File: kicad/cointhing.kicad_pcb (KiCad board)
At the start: 4 copper layers, 30 x 30 mm, 24 parts, among them J1 USB_B_Micro, Q1 PUMX1, Q2 S8050_J3Y, U1 ESP-12E, U2 CP2102-GMR_NRND, U3 BL8565, U4 74AHC1G08

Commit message: second pcb
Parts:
- removed LED1: WS2812B, LED_SMD:LED_WS2812B_PLCC4_5.0x5.0mm_P3.2mm
- added D1: WS2812B-2020, barn53-kicad:WS2812B-2020, B.Cu at (162.5, 71.0)
- added REF**: hole, hole, F.Cu at (154.5, 63.0)
- C4, C6, C7, C8, C9, R1, R3: moved to F.Cu
- moved R7 60.3 mm to (148.5, 78.0)
- moved U4 60.3 mm to (148.5, 81.0)
- moved J1 52.5 mm to (162.5, 60.1)
- moved C5 51.4 mm to (166.0, 73.5), turned to 90 degrees
- moved C2 50.9 mm to (175.0, 61.0)
- moved C3 50.9 mm to (175.0, 59.0)
- moved U1 48.3 mm to (165.5, 77.0), turned to 270 degrees
- moved C1 47.5 mm to (171.5, 59.0), turned to 0 degrees
- moved U2 44.6 mm to (174.5, 60.5), turned to 180 degrees
- moved Q1 43.8 mm to (167.0, 65.5)
- moved D2 42.6 mm to (162.5, 78.0)
- moved C6 41.1 mm to (148.5, 69.5), turned to 180 degrees
- moved C7 41.1 mm to (148.5, 67.5), turned to 180 degrees
- moved Q2 40.2 mm to (171.5, 69.0), turned to 90 degrees
- moved R6 40.1 mm to (172.5, 73.5), turned to 270 degrees
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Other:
- board size 30 x 30 mm -> 35 x 32 mm

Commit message: Wired PCB rev.B
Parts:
- added QR*****: https://barn53.github.io/CoinThing/, https://barn53.github.io/CoinThing/, B.Cu at (152.5, 76.9)
- moved C3 10.9 mm to (168.7, 67.9)
- moved R6 9.63 mm to (165.4, 80.0)
- moved C2 7.98 mm to (168.7, 65.9)
- moved D2 7.50 mm to (162.5, 85.5)
- moved C5 7.20 mm to (162.9, 80.0)
- moved Q2 7.20 mm to (168.4, 75.5)
- moved R5 7.20 mm to (167.4, 80.0)
- moved R4 6.56 mm to (169.4, 80.0)
- moved C1 5.64 mm to (168.7, 63.9), turned to 180 degrees
- moved U1 1.70 mm to (165.5, 78.7)
- moved C4 1.00 mm to (148.5, 72.5)
- moved C6 1.00 mm to (148.5, 70.5)
- moved C7 1.00 mm to (148.5, 68.5)
- moved C8 1.00 mm to (148.5, 66.5)
- moved C9 1.00 mm to (148.5, 64.5)
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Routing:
- net +3V3: track 0.00 -> 74.9 mm, vias 0 -> 6
- net VBUS: track 0.00 -> 58.8 mm, vias 0 -> 7
- net /TxD: track 0.00 -> 51.0 mm, vias 0 -> 4
- net /VDD: track 0.00 -> 32.7 mm, vias 0 -> 5
- net /~Reset: track 0.00 -> 30.9 mm, vias 0 -> 3
- net Net-(R1-Pad8): track 0.00 -> 30.6 mm, vias 0 -> 2
- net /GPIO0: track 0.00 -> 30.2 mm, vias 0 -> 2
- net /GPIO5: track 0.00 -> 28.9 mm, vias 0 -> 2
- net /RxD: track 0.00 -> 26.7 mm
- net Net-(R1-Pad5): track 0.00 -> 25.1 mm, vias 0 -> 2
- net /~TFT_RES: track 0.00 -> 25.0 mm, vias 0 -> 1
- net Net-(D1-Pad3): track 0.00 -> 22.1 mm, vias 0 -> 1
- net /DTR: track 0.00 -> 20.6 mm, vias 0 -> 4
- net /D-: track 0.00 -> 19.9 mm, vias 0 -> 2
- net /TFT_SDA: track 0.00 -> 19.6 mm, vias 0 -> 1
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- added copper zone on B.Cu, net GND
- added copper zone on F.Cu, net GND
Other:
- board size 35 x 32 mm -> 35 x 34 mm
- copper layers 4 -> 2
- net class Default: via_dia 0.6 -> 0.45; via_drill 0.3 -> 0.2
- net class Power: clearance 0.254 -> 0.1524
- board text added: "CoinThing a coin ticker display"
- board text added: "CoinThing barn53 rev.B 02/21"
- board text added: "To the Moon!"

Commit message: Rev.B PCB
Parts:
- QR*****: footprint https://barn53.github.io/CoinThing/ -> https:__barn53.github.io_CoinThing_
- moved U3 2.10 mm to (149.0, 61.6)
- moved C4 1.80 mm to (148.5, 74.3)
- moved C6 1.80 mm to (148.5, 72.3)
- moved C7 1.80 mm to (148.5, 70.3)
- moved C8 1.80 mm to (148.5, 68.3)
- moved C9 1.80 mm to (148.5, 66.3)
- moved J1 0.18 mm to (162.5, 59.9)
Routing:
- net VBUS: track 58.8 -> 61.8 mm
- net Net-(R1-Pad6): track 17.1 -> 18.4 mm
- net Net-(D1-Pad3): track 22.1 -> 20.9 mm
- net Net-(R1-Pad5): track 25.1 -> 26.1 mm
- net /~Reset: track 30.9 -> 31.9 mm
- net +3V3: track 74.9 -> 75.7 mm
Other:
- outline, holes or cut-outs redrawn
- board text added: "CoinThing"

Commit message: Added second mounting hole to PCB, rearranged parts a bit
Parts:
- added REF**: hole, hole, F.Cu at (175.0, 59.9)
- moved U3 5.70 mm to (154.5, 63.1)
- moved REF** 5.46 mm to (150.0, 59.9)
- moved U2 4.55 mm to (175.2, 65.9)
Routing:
- net Net-(R1-Pad8): track 31.0 -> 25.4 mm
- net /RTS: track 16.1 -> 21.4 mm, vias 2 -> 5
- net VBUS: track 61.8 -> 56.9 mm, vias 7 -> 8
- net /D+: track 18.5 -> 23.2 mm, vias 2 -> 4
- net /RxD: track 26.7 -> 23.0 mm
- net /TxD: track 51.0 -> 47.3 mm
- net +3V3: track 75.7 -> 78.8 mm, vias 6 -> 7
- net /D-: track 20.0 -> 21.9 mm, vias 2 -> 4
- net Net-(R1-Pad5): track 26.1 -> 25.5 mm
- net /VDD: track 32.7 -> 33.3 mm
- net /GPIO0: track 30.2 -> 30.7 mm
- net GND: vias 6 -> 13
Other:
- board text added: "CoinThing barn53 rev.C 02/21"
- board text removed: "CoinThing barn53 rev.B 02/21"

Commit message: modified PCB wiring
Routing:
- net /VDD: track 33.3 -> 29.4 mm, vias 5 -> 4
- net Net-(R1-Pad6): track 18.3 -> 14.7 mm, vias 4 -> 2
- net +3V3: track 78.8 -> 77.3 mm, vias 7 -> 8

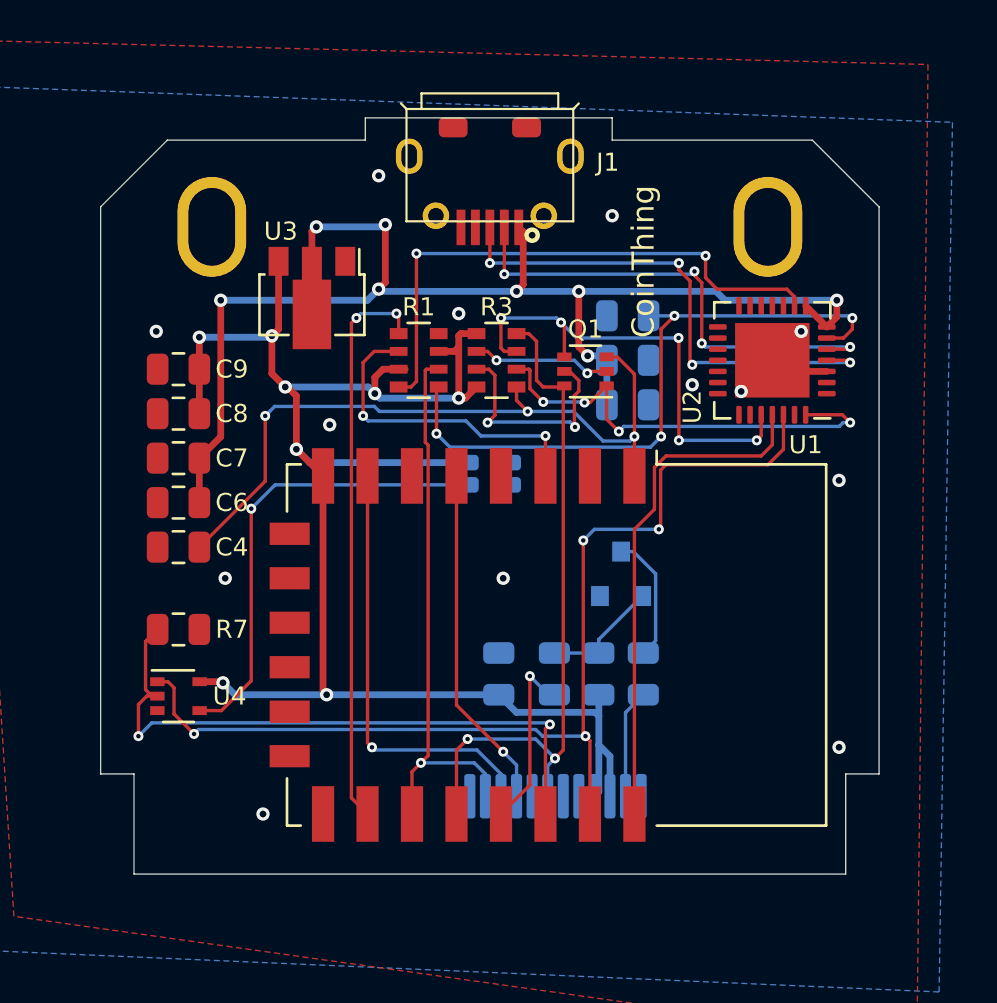
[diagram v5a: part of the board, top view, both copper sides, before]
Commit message: PCB completely new part arrangement
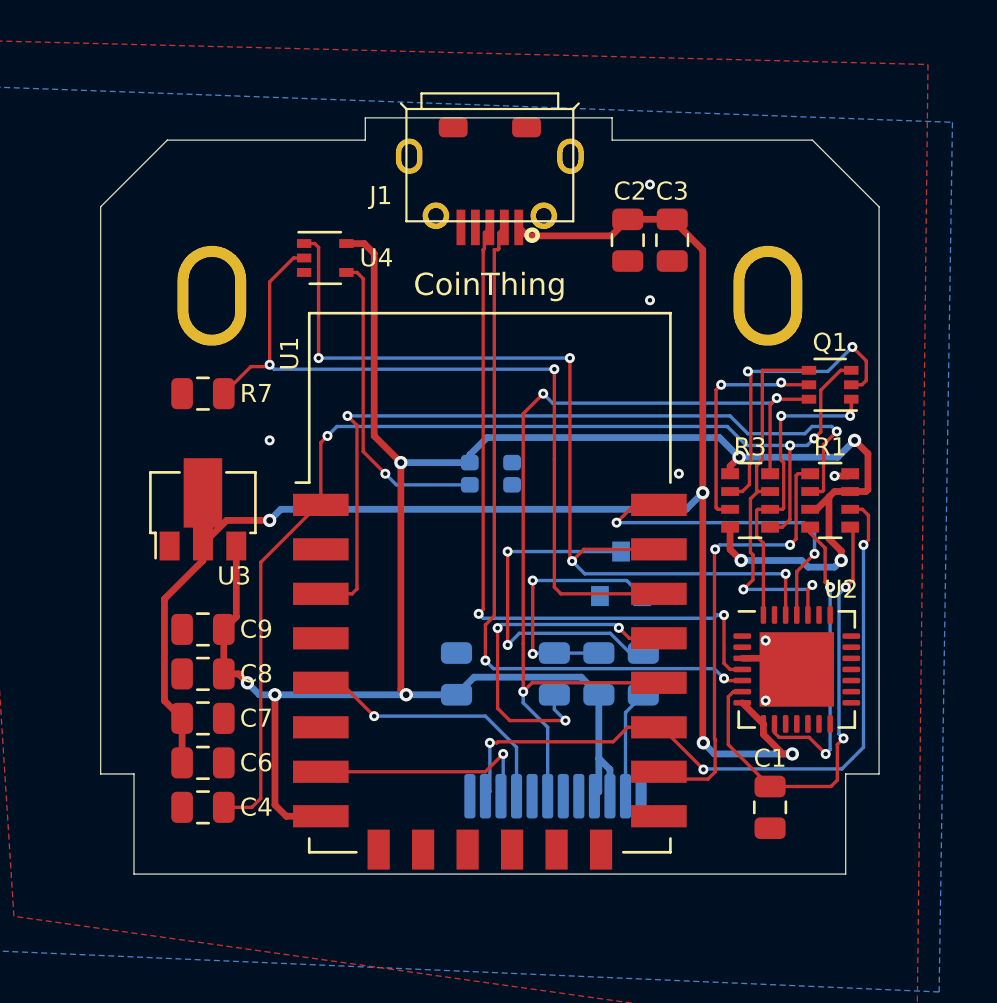
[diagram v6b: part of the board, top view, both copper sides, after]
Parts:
- C1, C2, C3: moved to F.Cu
- moved C1 23.0 mm to (175.1, 86.0), turned to 270 degrees
- moved U4 20.8 mm to (155.1, 61.3)
- moved R1 19.5 mm to (177.8, 72.2)
- moved U2 13.9 mm to (176.3, 79.8), turned to 0 degrees
- moved R3 13.0 mm to (174.2, 72.2)
- moved C4 11.8 mm to (149.6, 86.0)
- moved C6 11.8 mm to (149.6, 84.0), turned to 0 degrees
- moved C7 11.8 mm to (149.6, 82.0), turned to 0 degrees
- moved C8 11.8 mm to (149.6, 80.0)
- moved C9 11.8 mm to (149.6, 78.0)
- moved Q1 11.0 mm to (177.8, 67.0)
- moved U3 10.7 mm to (149.6, 72.6), turned to 90 degrees
- moved R7 10.7 mm to (149.6, 67.4), turned to 180 degrees
- moved C3 7.67 mm to (170.7, 60.5), turned to 270 degrees
- moved C2 5.40 mm to (168.7, 60.5), turned to 270 degrees
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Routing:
- net Net-(R1-Pad6): track 14.7 -> 35.8 mm
- net +3V3: track 77.3 -> 97.2 mm
- net /~Reset: track 32.1 -> 50.4 mm
- net VBUS: track 57.3 -> 73.5 mm, vias 8 -> 4
- net Net-(R1-Pad8): track 25.4 -> 13.7 mm
- net Net-(Q2-Pad3): track 5.76 -> 16.0 mm, vias 0 -> 2
- net /GPIO0: track 30.7 -> 41.0 mm, vias 2 -> 3
- net /D-: track 21.9 -> 31.8 mm, vias 4 -> 2
- net /TFT_SDA: track 19.6 -> 10.5 mm
- net /VDD: track 29.4 -> 20.6 mm, vias 4 -> 2
- net /D+: track 23.2 -> 31.9 mm, vias 4 -> 2
- net /RxD: track 23.0 -> 15.3 mm, vias 0 -> 2
- net /TFT_BL: track 8.19 -> 15.8 mm, vias 1 -> 3
- net Net-(Q1-Pad2): track 6.29 -> 13.8 mm
- net /~TFT_RES: track 25.0 -> 32.2 mm, vias 1 -> 3
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
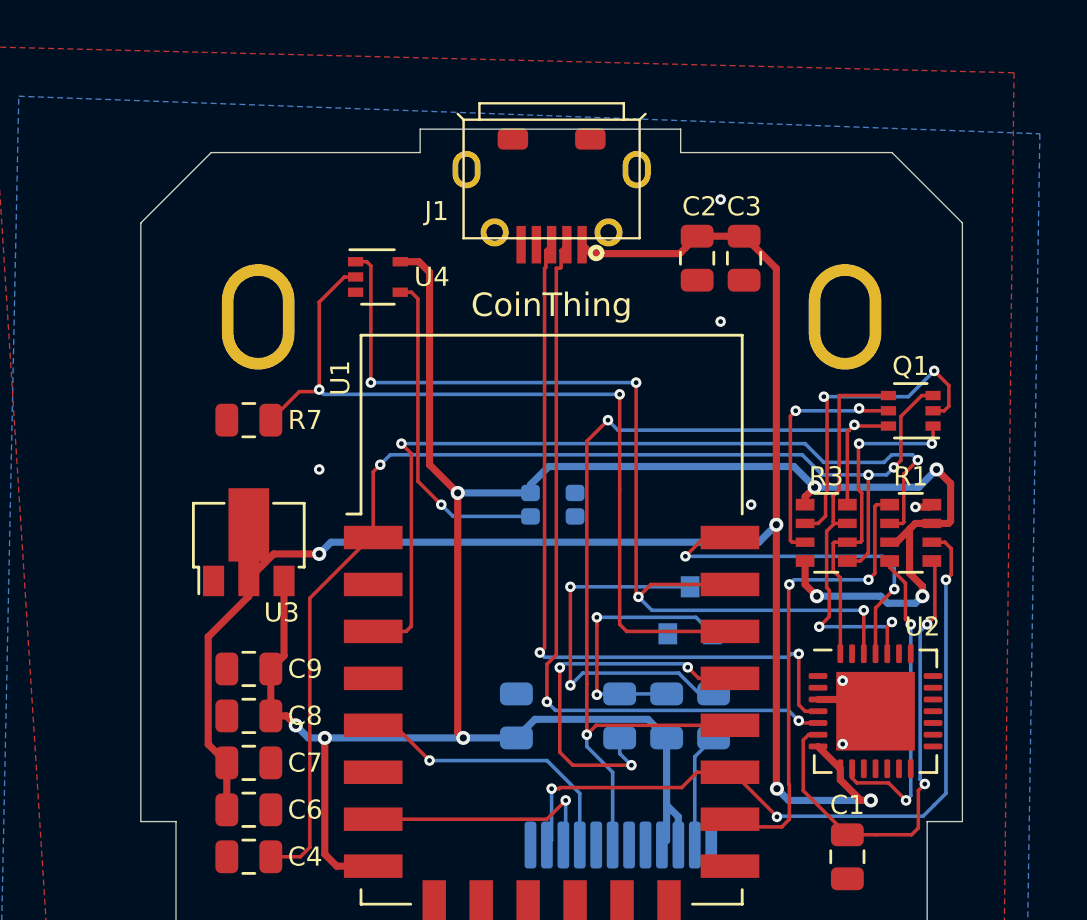
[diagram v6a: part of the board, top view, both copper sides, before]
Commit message: Moved USB to the side
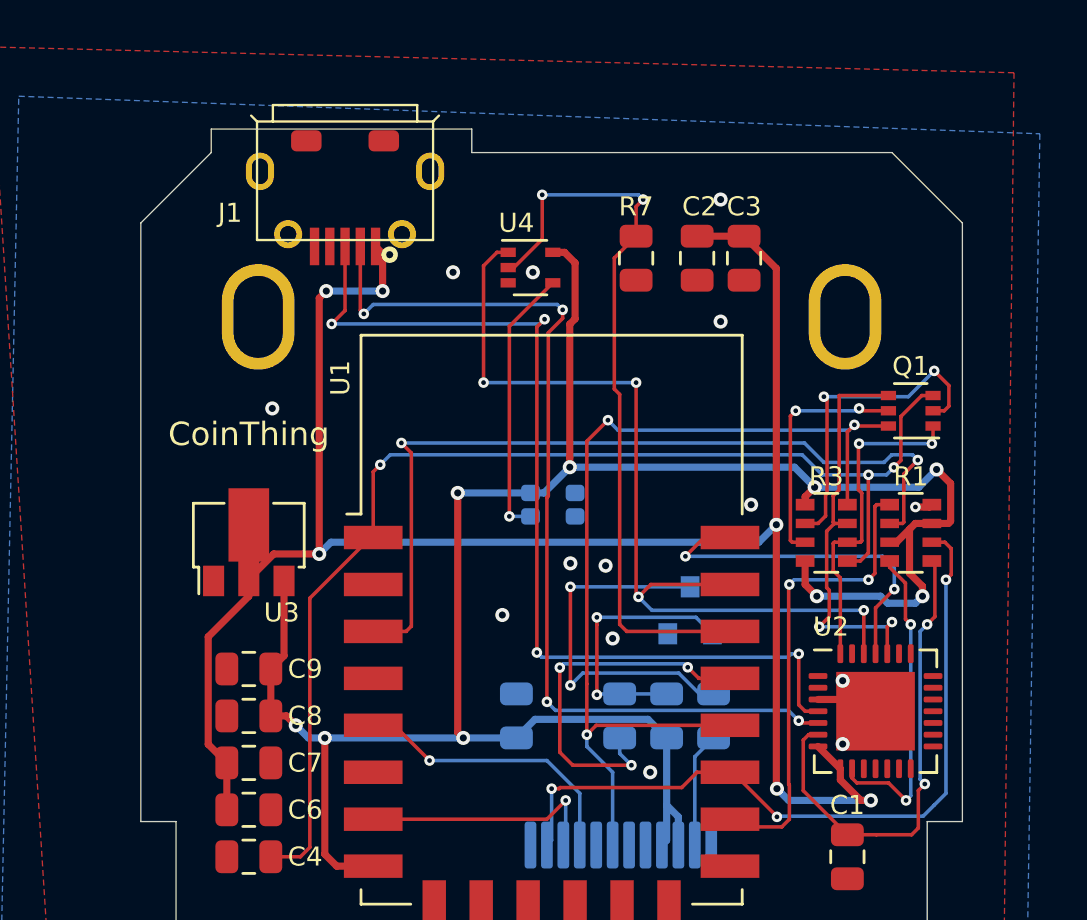
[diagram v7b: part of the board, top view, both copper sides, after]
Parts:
- moved R7 17.9 mm to (166.1, 60.5), turned to 270 degrees
- moved J1 8.80 mm to (153.7, 60.0)
- moved U4 6.51 mm to (161.6, 60.9)
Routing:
- net VBUS: track 73.5 -> 83.9 mm, vias 4 -> 6
- net /D+: track 31.9 -> 41.5 mm, vias 2 -> 4
- net /D-: track 31.8 -> 40.6 mm, vias 2 -> 4
- net /TxD: track 42.0 -> 37.7 mm
- net /GPIO5: track 35.8 -> 31.8 mm
- net Net-(D1-Pad3): track 14.1 -> 11.6 mm
- net +3V3: track 97.2 -> 95.5 mm, vias 8 -> 9
- net GND: vias 7 -> 14
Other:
- outline, holes or cut-outs redrawn

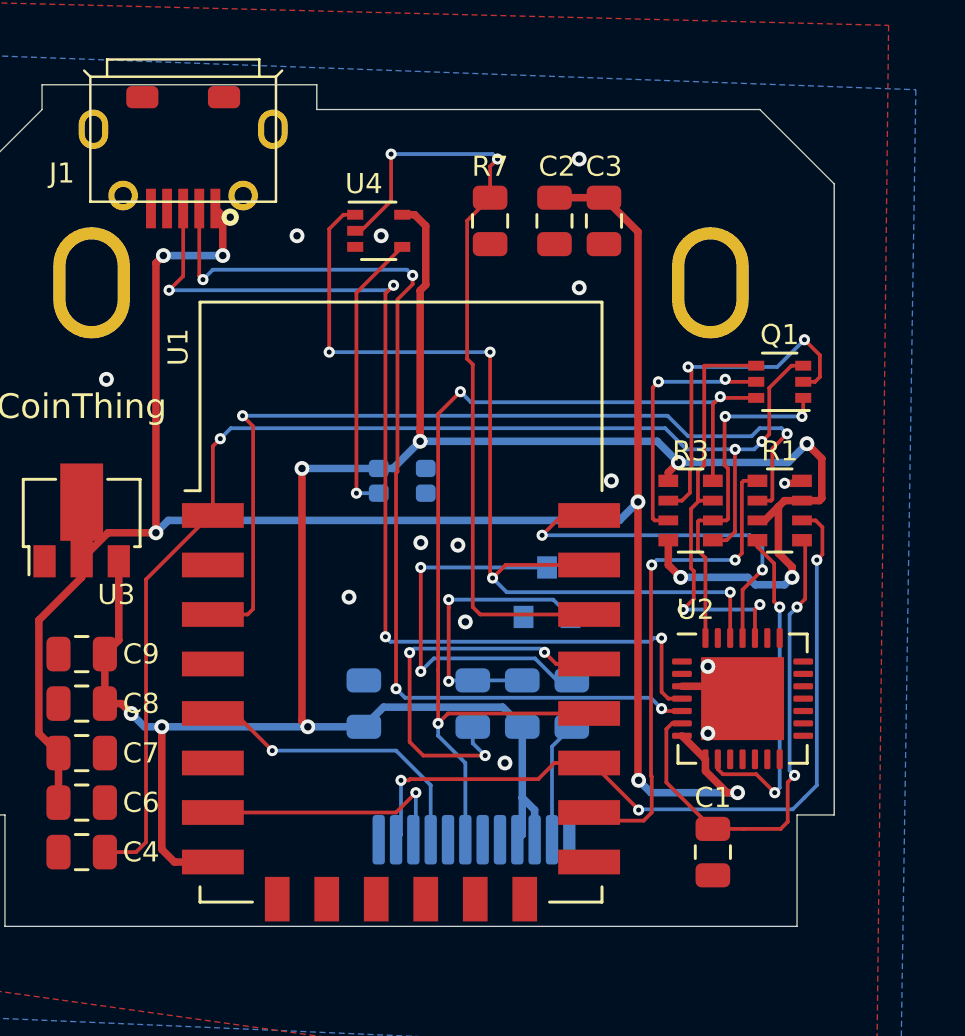
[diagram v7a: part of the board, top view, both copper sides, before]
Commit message: moved led to the center of the bottom plane
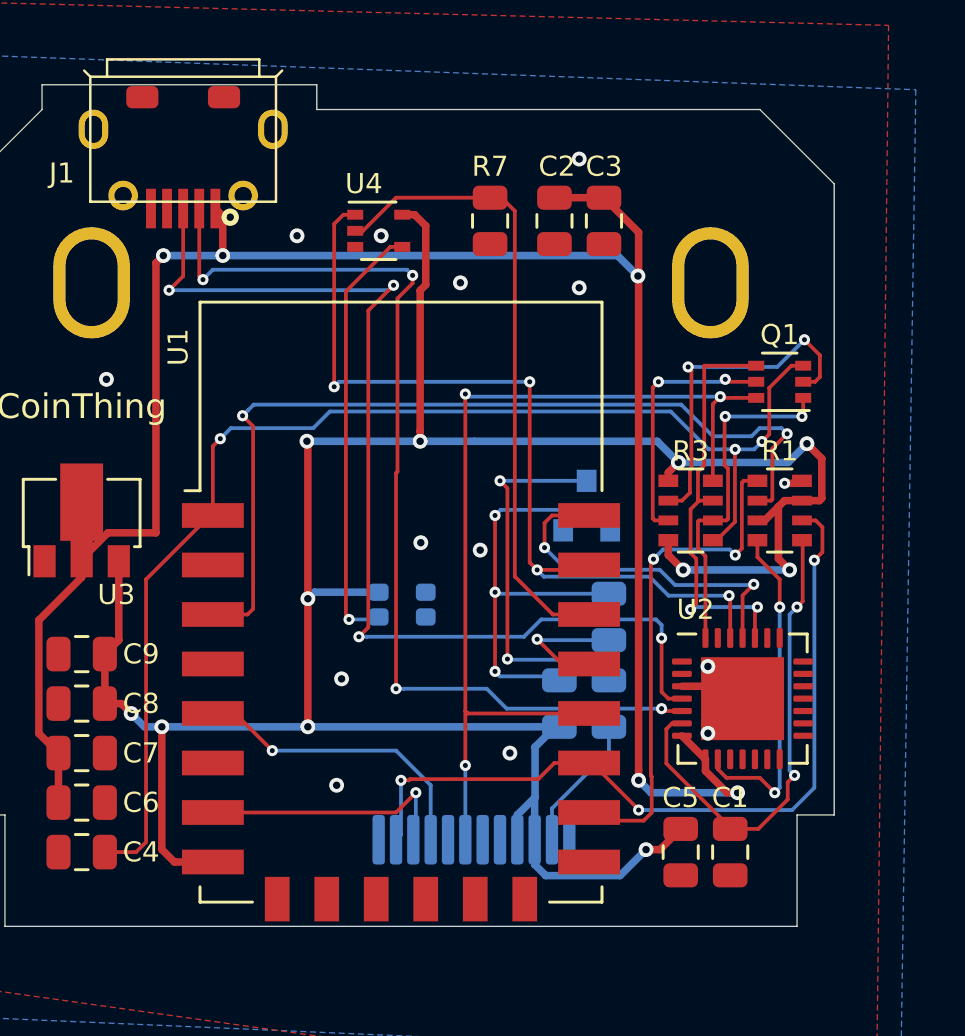
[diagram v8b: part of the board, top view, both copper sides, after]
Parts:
- C5: moved to F.Cu
- moved C5 14.1 mm to (173.8, 86.0), turned to 270 degrees
- moved R6 6.52 mm to (170.9, 76.5)
- moved D1 5.00 mm to (162.5, 76.0)
- moved Q2 3.85 mm to (170.0, 72.0)
- moved R4 1.50 mm to (170.9, 80.0)
- moved R5 1.50 mm to (168.9, 80.0)
- moved C1 0.70 mm to (175.8, 86.0)
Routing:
- net +3V3: track 95.5 -> 107.0 mm, vias 9 -> 11
- net /TFT_BL: track 15.8 -> 5.46 mm, vias 3 -> 1
- net Net-(Q2-Pad1): track 11.5 -> 19.0 mm, vias 2 -> 3
- net /GPIO5: track 31.8 -> 25.6 mm, vias 2 -> 0
- net Net-(D1-Pad3): track 11.6 -> 17.6 mm
- net VBUS: track 83.9 -> 81.0 mm, vias 6 -> 5
- net /GPIO0: track 41.0 -> 38.4 mm
- net /TxD: track 37.7 -> 35.4 mm
- net /D+: track 41.5 -> 43.8 mm
- net /VDD: track 20.6 -> 19.5 mm
- net /RxD: track 15.3 -> 14.4 mm
- net Net-(Q2-Pad3): track 16.0 -> 15.3 mm
- net /LEDK: track 4.89 -> 5.52 mm
- net /RTS: track 17.6 -> 17.0 mm
